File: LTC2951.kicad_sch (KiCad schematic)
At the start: 21 parts, among them SW3 SW_Push, U3 LTC2951ITS8-1

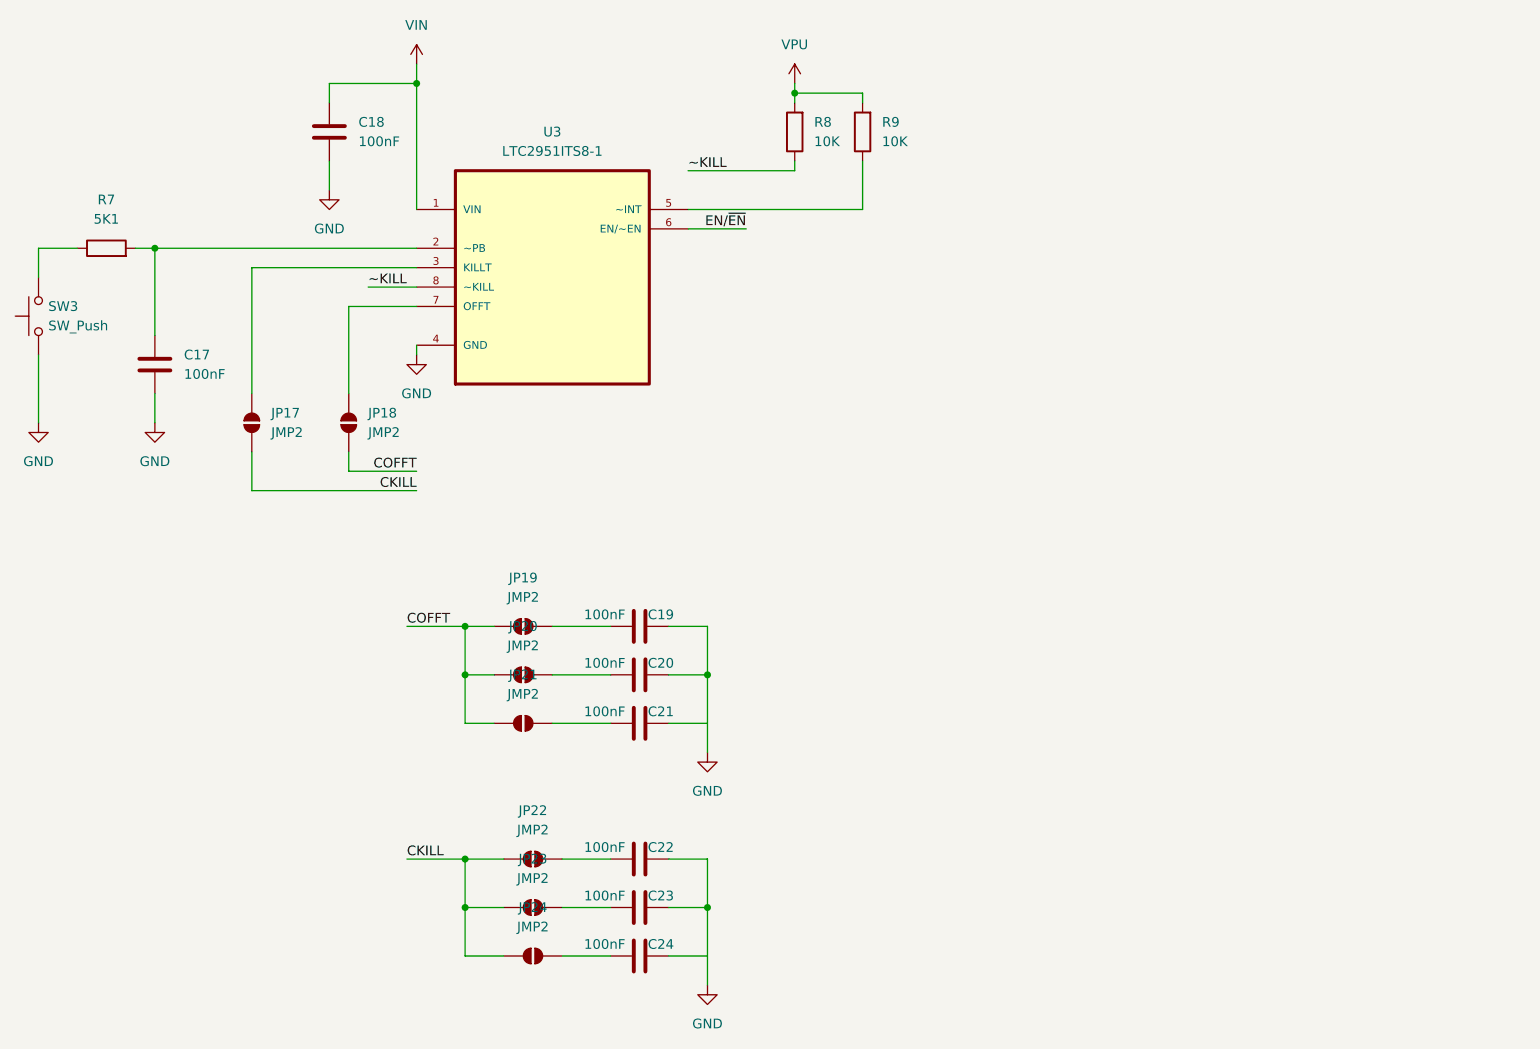
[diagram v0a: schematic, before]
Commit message: Added B.O.M, TODO: do PCB track layout
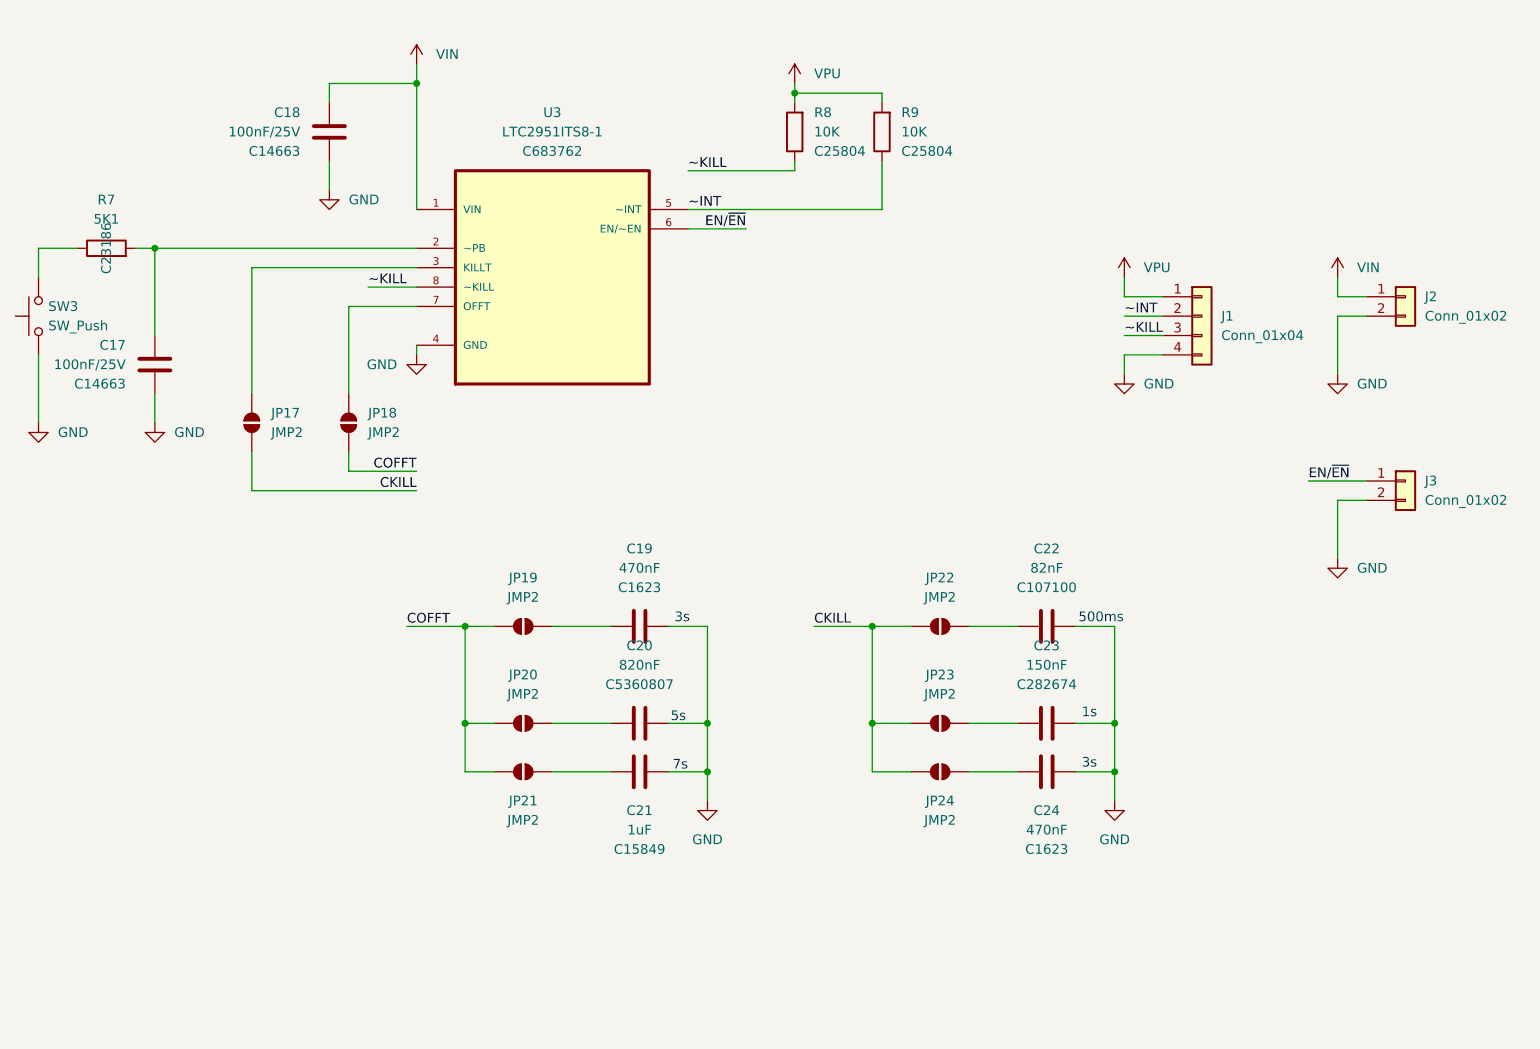
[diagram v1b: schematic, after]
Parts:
- added J1: Conn_01x04, Connector_PinHeader_2.54mm:PinHeader_1x04_P2.54mm_Vertical, symbol Connector_Generic:Conn_01x04
- added J2, J3: Conn_01x02, Connector_PinHeader_2.54mm:PinHeader_1x02_P2.54mm_Vertical, symbol Connector_Generic:Conn_01x02
- C17, C18: value 100nF -> 100nF/25V; JLCPCB Part # (none) -> C14663
- C19, C24: value 100nF -> 470nF; JLCPCB Part # (none) -> C1623
- C20: value 100nF -> 820nF; JLCPCB Part # (none) -> C5360807
- C21: value 100nF -> 1uF; JLCPCB Part # (none) -> C15849
- C22: value 100nF -> 82nF; JLCPCB Part # (none) -> C107100
- C23: value 100nF -> 150nF; JLCPCB Part # (none) -> C282674
- R7: JLCPCB Part # (none) -> C23186
- R8, R9: JLCPCB Part # (none) -> C25804
- U3: JLCPCB Part # (none) -> C683762
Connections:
- net EN/~{EN}: now also J3.1 (Pin_1)
- net GND: now also C21.2, C24.2, J1.4 (Pin_4), J2.2 (Pin_2), J3.2 (Pin_2)
- net VIN: now also J2.1 (Pin_1)
- net VPU: now also J1.1 (Pin_1)
- net ~KILL: now also J1.3 (Pin_3)
- net ~INT: now reaches R9.1, U3.5 (~INT)
- net ~INT: now also J1.2 (Pin_2)
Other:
- note added: "1s"
- note added: "3s"
- note added: "500ms"
- note added: "5s"
- note added: "7s"
- moved on the sheet: C20, C21, C22, C23, C24, JP20, JP21, JP22, JP23, JP24, R9

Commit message: Finished, 1st PCB order to JLCPCB
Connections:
- net VIN renamed VIN_2951
- net VPU renamed VPU_2951
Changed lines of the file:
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@@
 			)
 		)
-		(property "Value" "VIN"
-			(at 134.62 27.9399 0)
-			(effects
-				(font
-					(size 1.27 1.27)
-				)
-				(justify left)
+		(property "Value" "VIN_2951"
+			(at 132.08 24.13 0)
+			(effects
+				(font
+					(size 1.27 1.27)
+				)
 			)
 		)
@@
 			)
 		)
-		(property "Value" "VIN"
-			(at 255.27 55.8799 0)
-			(effects
-				(font
-					(size 1.27 1.27)
-				)
-				(justify left)
+		(property "Value" "VIN_2951"
+			(at 252.73 52.07 0)
+			(effects
+				(font
+					(size 1.27 1.27)
+				)
 			)
 		)
@@
 			)
 		)
-		(property "Value" "VPU"
-			(at 184.15 30.4799 0)
-			(effects
-				(font
-					(size 1.27 1.27)
-				)
-				(justify left)
+		(property "Value" "VPU_2951"
+			(at 181.61 26.67 0)
+			(effects
+				(font
+					(size 1.27 1.27)
+				)
 			)
 		)
@@
 			)
 		)
-		(property "Value" "VPU"
-			(at 227.33 55.8799 0)
-			(effects
-				(font
-					(size 1.27 1.27)
-				)
-				(justify left)
-			)
-		)
+		(property "Value" "VPU_2951"
+			(at 224.79 52.07 0)
+			(effects
+				(font
+					(size 1.27 1.27)
+				)
+			)
+		)
